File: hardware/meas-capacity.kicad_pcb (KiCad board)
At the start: 2 copper layers, 57.8 x 44.4 mm, 24 parts, among them J2 Probe1, J3 Probe2, J4 Probe3, J5 Probe4, J6 CAN1, J7 CAN2, P1 CONN_PROG+SER_AVR, Q1 BSS138, U1 ATMEGA168PA-AU, U2 MCP2515-E/SO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

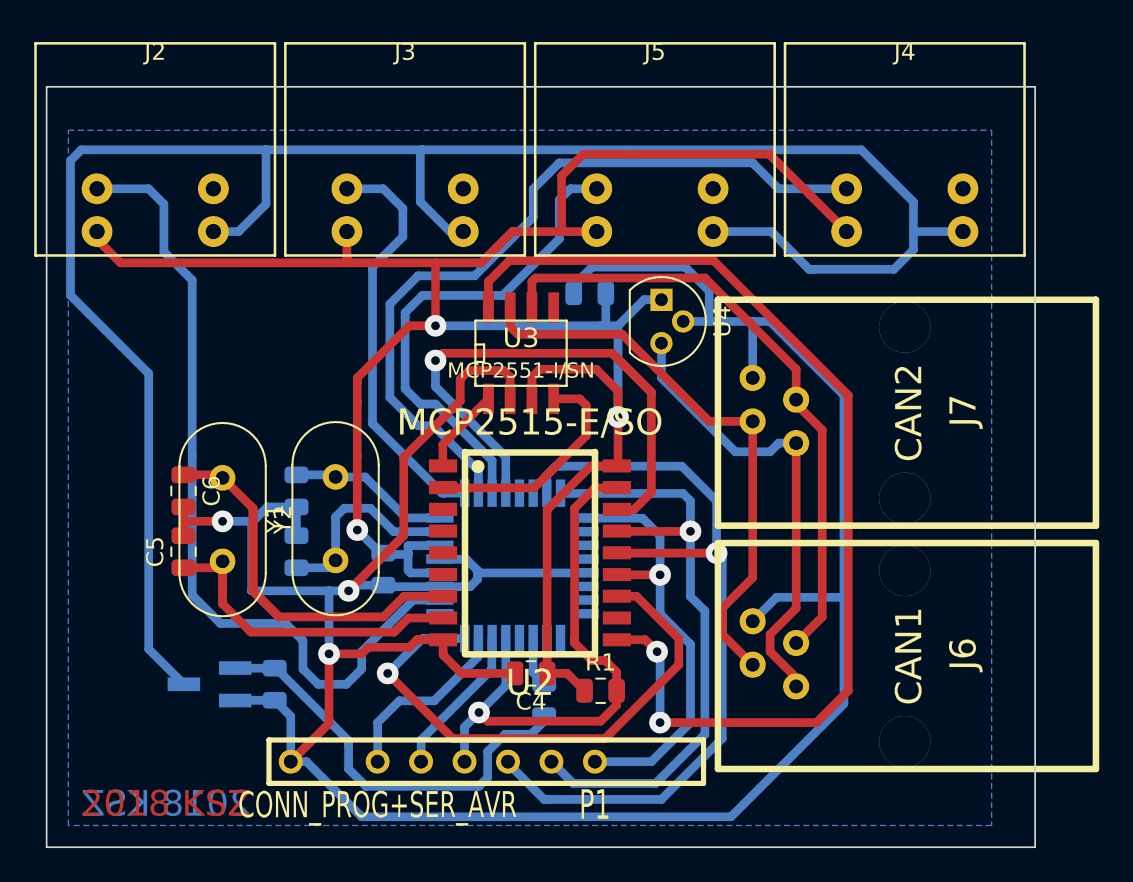
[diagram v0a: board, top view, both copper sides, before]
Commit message: Connect screen of Mini-DIN plug to GND
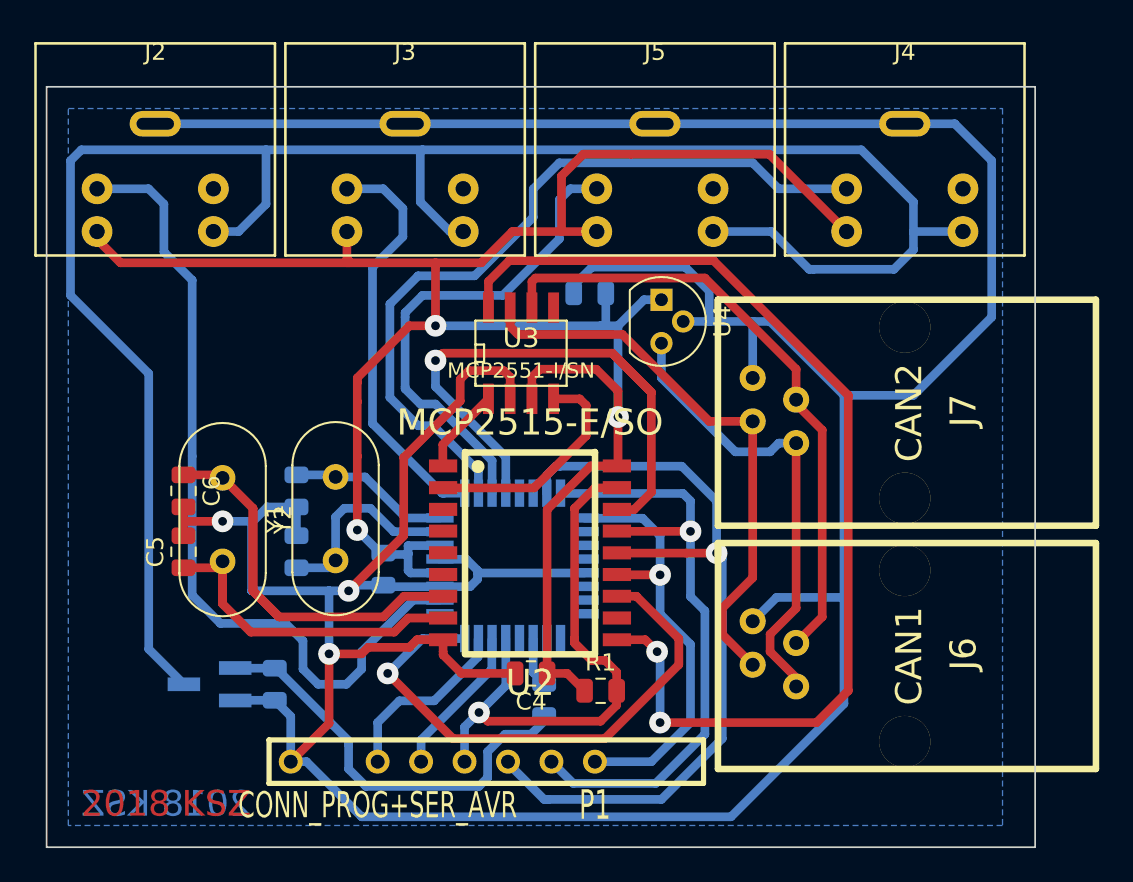
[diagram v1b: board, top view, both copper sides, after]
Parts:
- C5, C6: value 22p -> 33p
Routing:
- net GNDD: track 178.3 -> 247.8 mm

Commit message: Fix conflicting capacitor placement
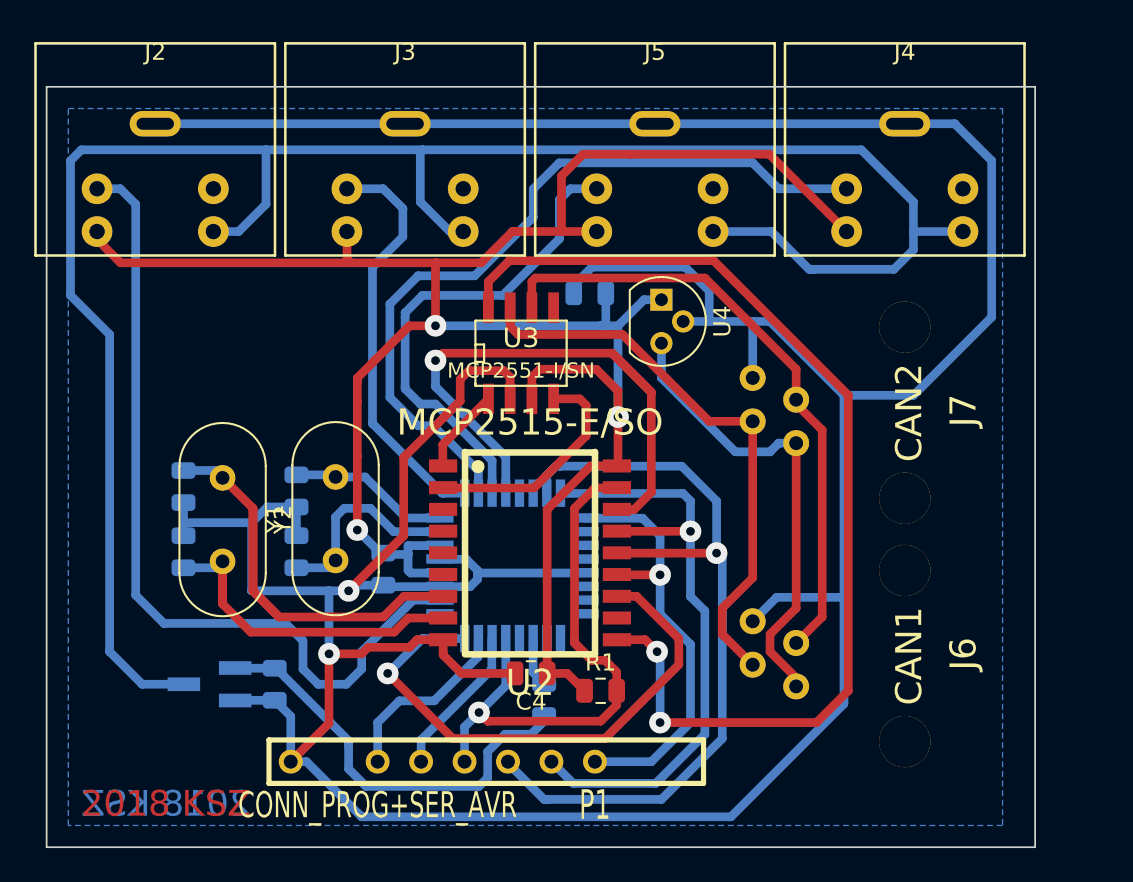
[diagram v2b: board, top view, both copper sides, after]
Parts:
- C5, C6: moved to B.Cu
- moved C6 0.25 mm to (224.5, 136.4)
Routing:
- net Net-(J2-Pad4): track 116.2 -> 117.7 mm
- net Net-(J2-Pad1): track 48.1 -> 49.0 mm
- net GNDD: track 247.8 -> 248.0 mm, vias 3 -> 2
